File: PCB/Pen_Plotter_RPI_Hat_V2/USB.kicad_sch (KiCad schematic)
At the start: 15 parts, among them Q1 NPN, Q2 NPN, Q3 NPN

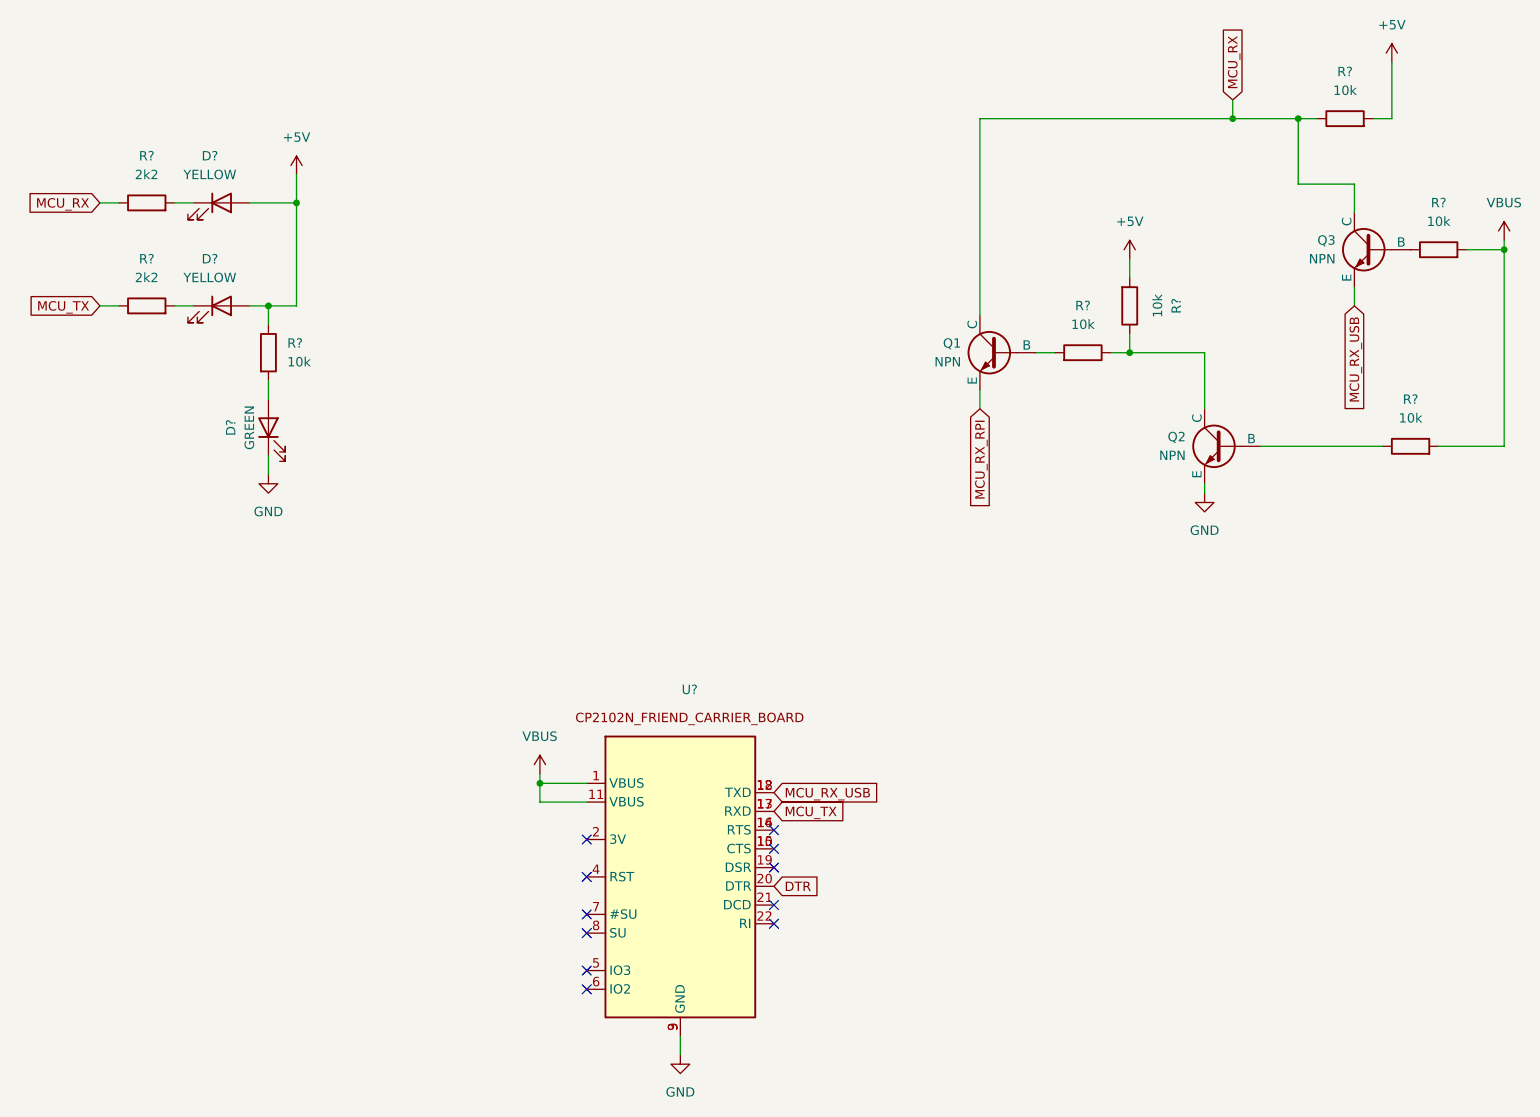
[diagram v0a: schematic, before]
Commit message: Simplified design, began layout process
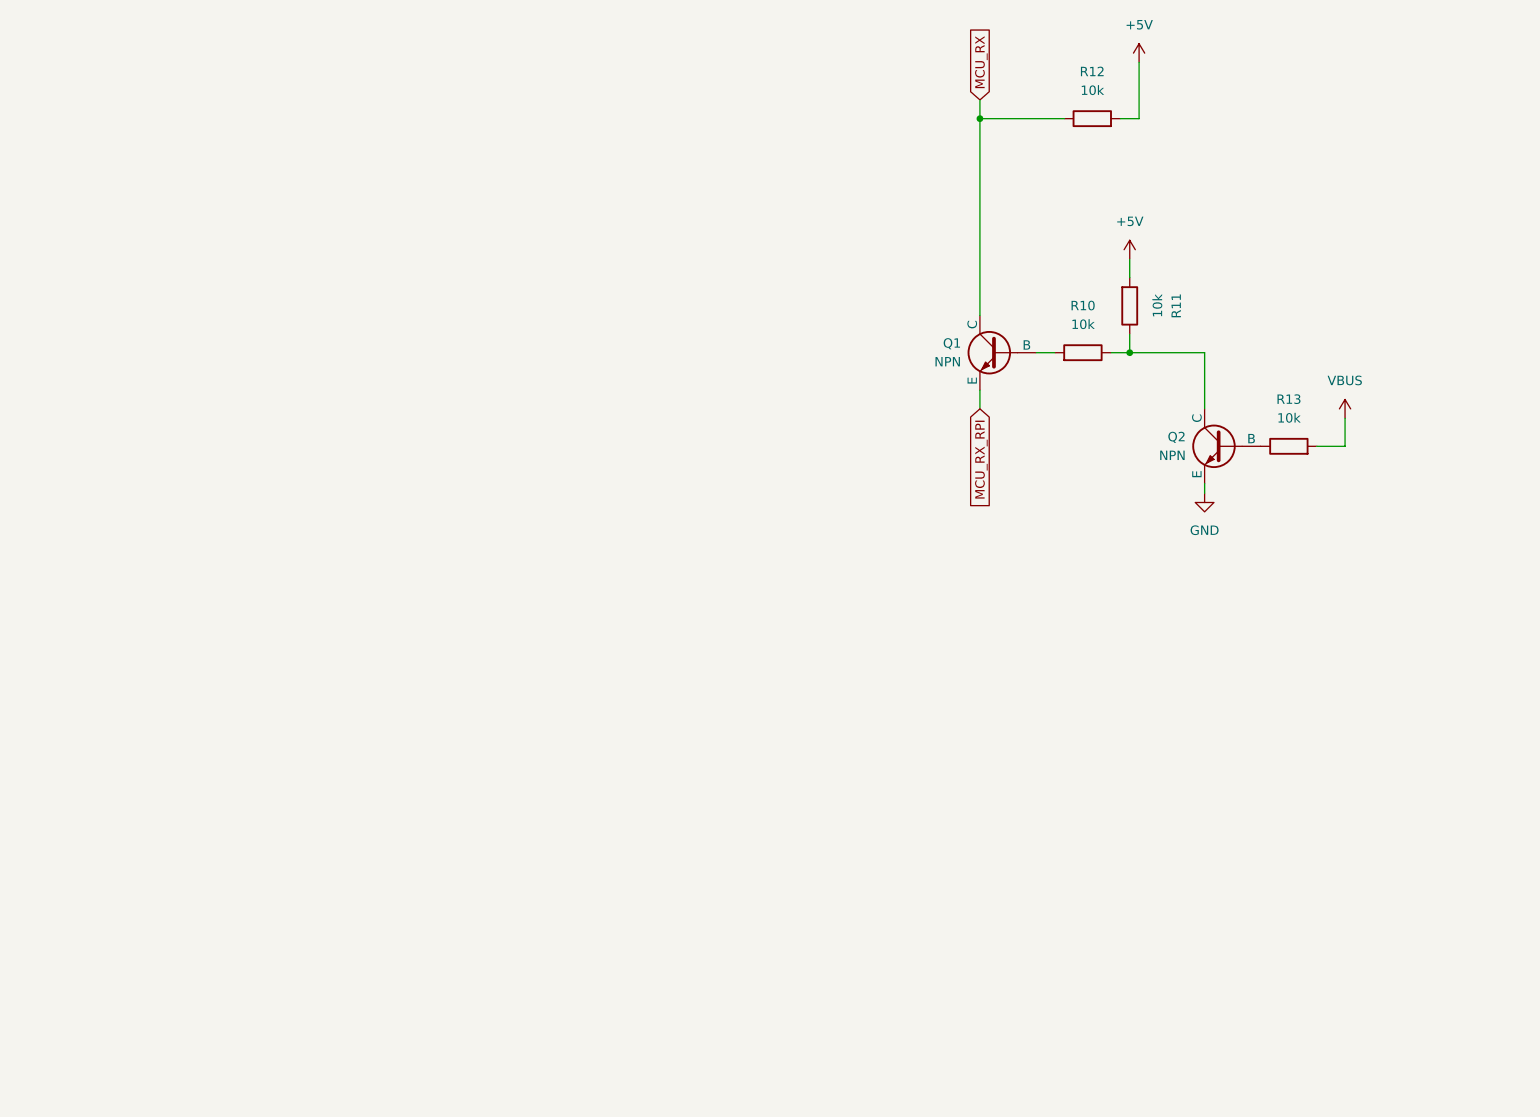
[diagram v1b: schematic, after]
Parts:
- removed D? (x2): YELLOW, LED_THT:LED_D5.0mm, symbol Device:LED
- removed D?: GREEN, LED_THT:LED_D5.0mm, symbol Device:LED
- removed Q3: NPN, symbol Simulation_SPICE:NPN
- removed R? (x2): 2k2, Pen_Plotter_Lib:THT_RESISTOR_WITH_VALUE, symbol Device:R
- removed R? (x2): 10k, Pen_Plotter_Lib:THT_RESISTOR_WITH_VALUE, symbol Device:R
- removed U?: ~, Pen_Plotter_Lib:CP2102N_FRIEND_CARRIER_BOARD_SMD, symbol Pen_Plotter_Lib:CP2102N_FRIEND_CARRIER_BOARD
- Q1: footprint (none) -> Capacitor_THT:CP_Radial_D5.0mm_P2.50mm
- gave numbers to parts that had none: 4
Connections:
- no-connect marks 11 -> 0
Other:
- moved on the sheet: R12, R13
